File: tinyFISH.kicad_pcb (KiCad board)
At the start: 2 copper layers, 20 x 20 mm, 89 parts, among them Q1 SI2302DS, U1 CC2510, U2 MPU-6000, U3 LP2985AIM5-3.0/NOPB, U4 STM32F303CCTx, U5 M25P16-VME, U6 MICRO_USB_B, U7 INA139, X1 26MHz, X2 8MHz

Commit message: fixed datestamp
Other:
- board text added: "01/2017"
- board text removed: "11/2016"

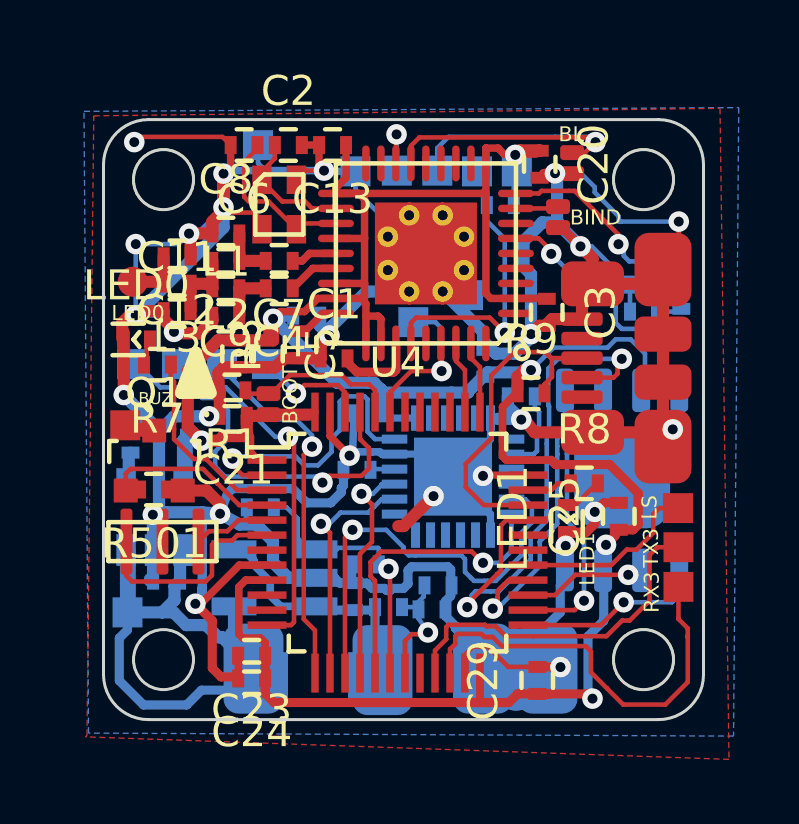
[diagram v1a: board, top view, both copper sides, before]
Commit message: added bind button
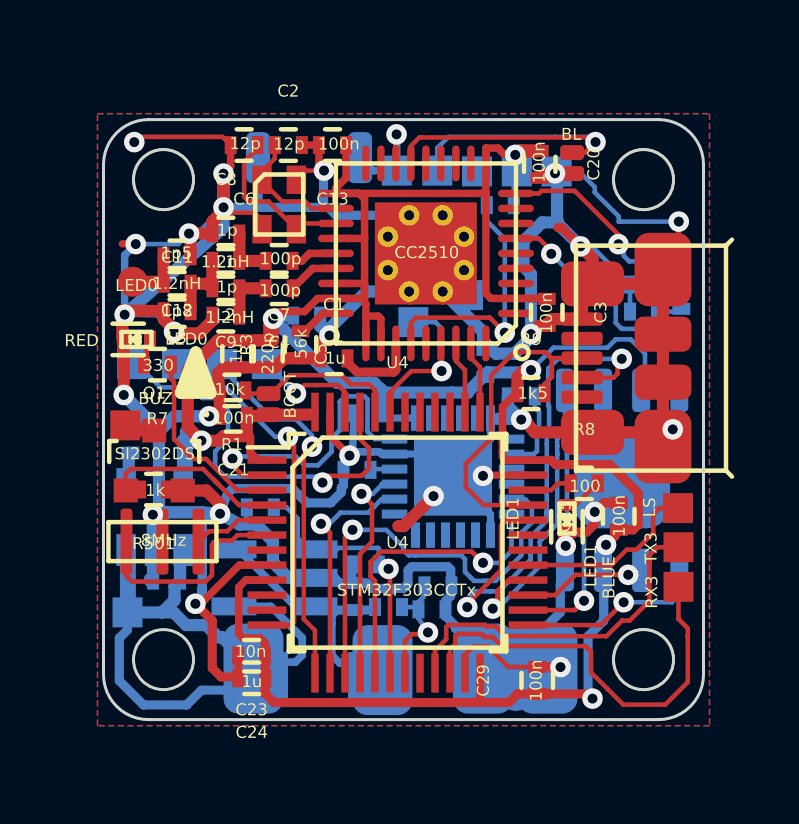
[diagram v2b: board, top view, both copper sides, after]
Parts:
- removed GND_MOUNT_1: GND, custom:TP_1x1
- BIND1: value BIND -> CUSTOM_PUSHBUTTON; footprint custom:SOLDERBRIDGE -> custom:OMRON_B3U-3000P; moved to B.Cu
- R4: value 330 -> 220
- R8: value 330 -> 100
- moved BIND1 8.53 mm to (25.5, 17.1), turned to 180 degrees
- moved ISP_GND1 6.71 mm to (33.7, 17.9)
- renumbered D1 to LED2, D2 to LED3
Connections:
- BIND1 pad 1: Net-(BIND1-Pad1) -> /rx/ISP_CLOCK
- U1 pad 8: Net-(BIND1-Pad1) -> Net-(U1-Pad8)
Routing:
- net GND: track 217.0 -> 224.6 mm
- net VBAT: track 21.6 -> 26.0 mm
- net /rx/ISP_CLOCK: track 2.24 -> 4.85 mm
- net /power/BAT+: track 9.75 -> 11.9 mm
- net Net-(BIND1-Pad1): track 1.43 -> 0.00 mm
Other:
- board text added: "BUZZER -"
- board text added: "BUZZER+"
- board text added: "CC 3V"
- board text added: "CC CLOCK"
- board text added: "CC DATA"
- board text added: "CC GND"
- board text added: "CC RESET"
- board text added: "ESC 0"
- board text added: "ESC 1"
- board text added: "ESC 2"
- board text added: "ESC 3"
- board text added: "FC BOOT"
- board text added: "G"
- board text added: "IN +"
- board text added: "IN -"
- board text added: "LED STRIP"
- board text added: "OUT +"
- board text added: "OUT -"
- board text added: "REV 0.2"
- board text added: "RX BIND"
- board text added: "RX BOOT"
- board text added: "RX DEBUG"
- board text added: "UART3 RX"
- board text added: "UART3 TX"
- board text added: "fishpepper.de/tinyFISH"
- board text removed: "VBAT"
